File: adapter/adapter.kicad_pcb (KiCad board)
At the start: 2 copper layers, 43.5 x 38.6 mm, 19 parts, among them J2 Conn_01x06_Female, SW1 RotaryEncoder_Switch

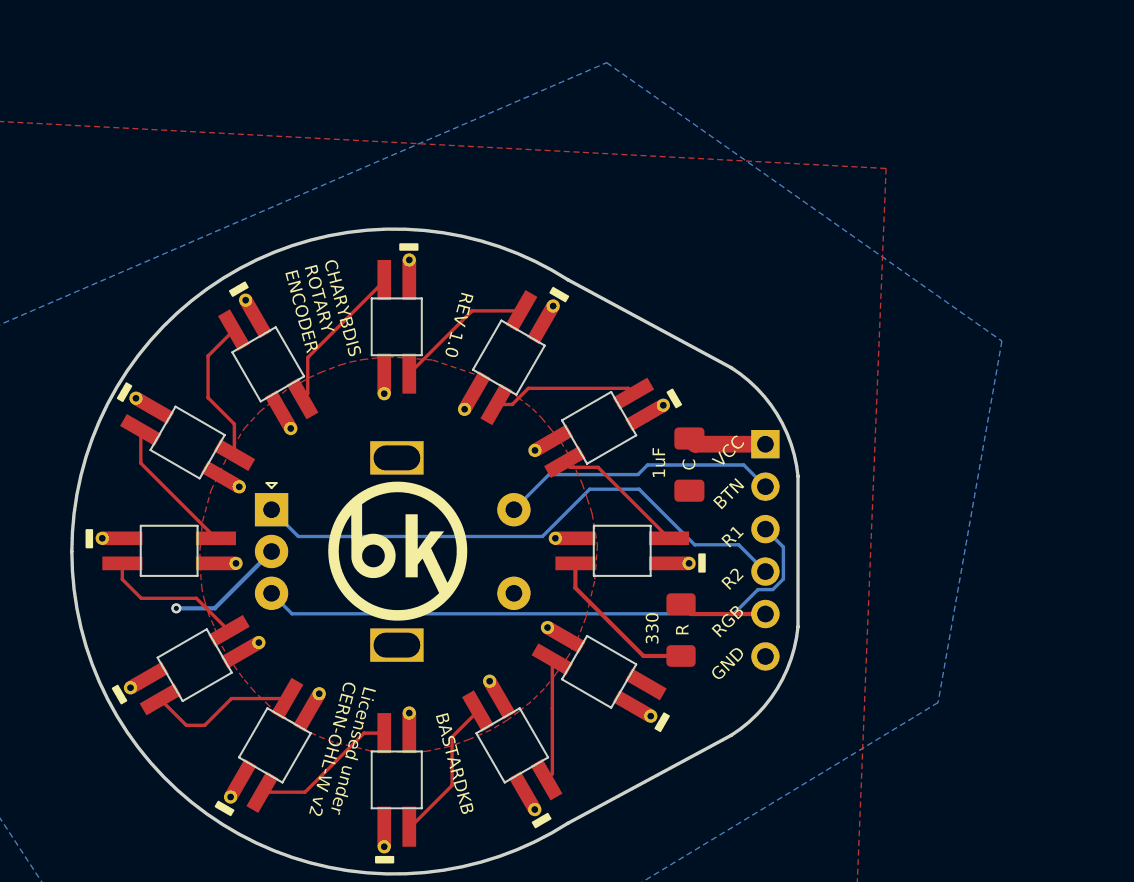
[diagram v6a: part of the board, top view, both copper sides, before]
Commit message: add screw holes
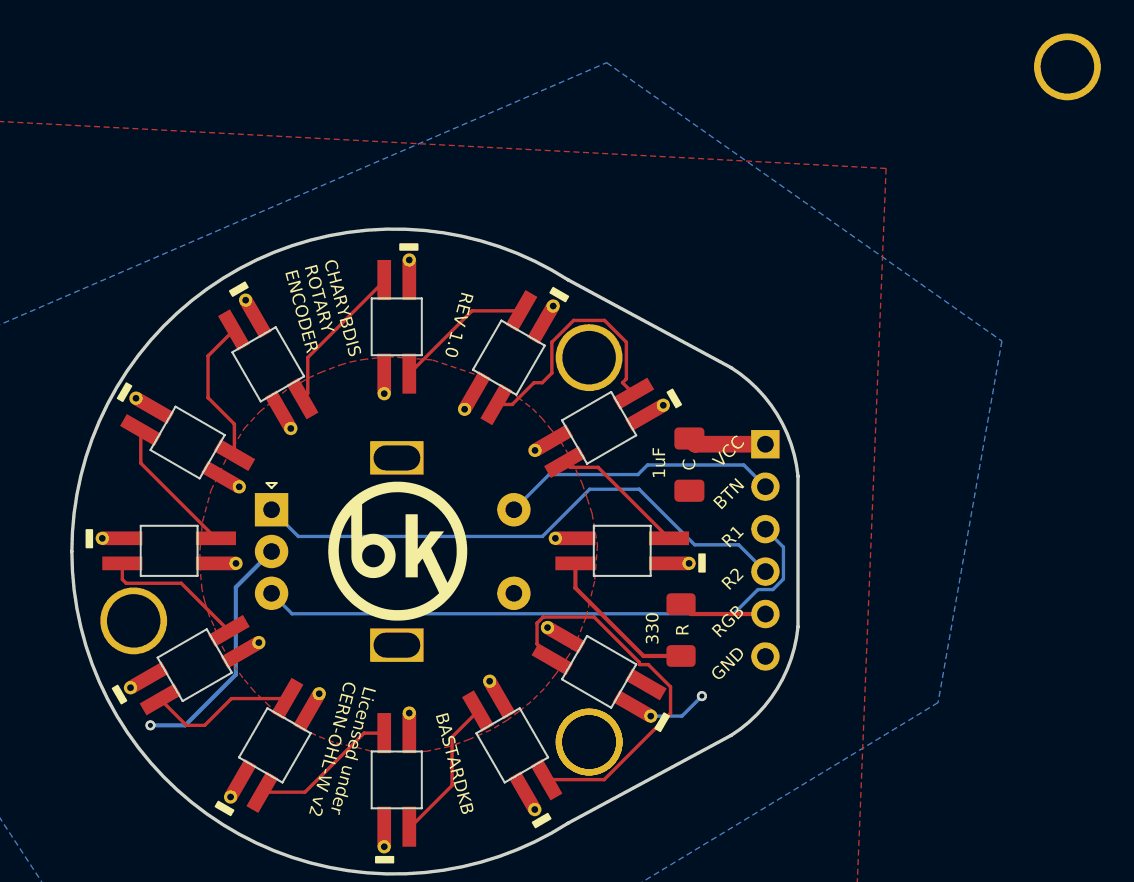
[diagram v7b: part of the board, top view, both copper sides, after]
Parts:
- added ? (x2): , , F.Cu at (64.0, 55.0)
- added ?: , , F.Cu at (92.6, 14.6)
- added ?: , , F.Cu at (36.8, 47.8)
- added ?: , , F.Cu at (64.0, 32.0)
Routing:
- net Net-(D11-Pad3): track 7.35 -> 23.1 mm
- net Gnd: track 7.11 -> 18.2 mm, vias 1 -> 2
- net Net-(D3-Pad1): track 8.73 -> 14.9 mm
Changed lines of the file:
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@@
       ) (layer "F.SilkS") (width 0) (fill solid))
+  )
+  (footprint "" (layer "F.Cu")
+    (at 64 55)
+    (fp_text reference "" (at 0 0) (layer "F.SilkS")
+      (effects (font (size 1.27 1.27) (thickness 0.15)))
+    )
+    (fp_text value "" (at 0 0) (layer "F.SilkS")
+      (effects (font (size 1.27 1.27) (thickness 0.15)))
+    )
+    (pad "1" thru_hole circle locked (at 0 0) (size 4 4) (drill 3.2) (layers *.Cu *.Mask))
   )
   (footprint "Library:YS-SK6812MINI-E" (layer "F.Cu")
@@
       (net 1 "Vcc") (pinfunction "VDD") (pintype "power_in"))
   )
+  (footprint "" (layer "F.Cu")
+    (at 92.62 14.6)
+    (fp_text reference "" (at 0 0) (layer "F.SilkS")
+      (effects (font (size 1.27 1.27) (thickness 0.15)))
+    )
+    (fp_text value "" (at 0 0) (layer "F.SilkS")
+      (effects (font (size 1.27 1.27) (thickness 0.15)))
+    )
+    (pad "1" thru_hole circle locked (at 0 0) (size 4 4) (drill 3.2) (layers *.Cu *.Mask))
+  )
   (footprint "Library:6_PinHeader" locked (layer "F.Cu")
     (at 74.55 43.6)
@@
       (net 1 "Vcc") (pinfunction "VDD") (pintype "power_in"))
   )
+  (footprint "" (layer "F.Cu")
+    (at 64 55)
+    (fp_text reference "" (at 0 0) (layer "F.SilkS")
+      (effects (font (size 1.27 1.27) (thickness 0.15)))
+    )
+    (fp_text value "" (at 0 0) (layer "F.SilkS")
+      (effects (font (size 1.27 1.27) (thickness 0.15)))
+    )
+    (pad "1" thru_hole circle locked (at 0 0) (size 4 4) (drill 3.2) (layers *.Cu *.Mask))
+  )
+  (footprint "" (layer "F.Cu")
+    (at 36.75 47.75)
+    (fp_text reference "" (at 0 0) (layer "F.SilkS")
+      (effects (font (size 1.27 1.27) (thickness 0.15)))
+    )
+    (fp_text value "" (at 0 0) (layer "F.SilkS")
+      (effects (font (size 1.27 1.27) (thickness 0.15)))
+    )
+    (pad "1" thru_hole circle locked (at 0 0) (size 4 4) (drill 3.2) (layers *.Cu *.Mask))
+  )
   (footprint "Resistor_SMD:R_1206_3216Metric_Pad1.30x1.75mm_HandSolder" (layer "F.Cu")
     (at 69.5 48.3 90)
@@
     (pad "4" thru_hole circle (at -4 -0.75 330) (size 0.8 0.8) (drill 0.4) (layers *.Cu *.Mask)
       (net 1 "Vcc") (pinfunction "VDD") (pintype "power_in"))
+  )
+  (footprint "" (layer "F.Cu")
+    (at 64 32)
+    (fp_text reference "" (at 0 0) (layer "F.SilkS")
+      (effects (font (size 1.27 1.27) (thickness 0.15)))
+    )
+    (fp_text value "" (at 0 0) (layer "F.SilkS")
+      (effects (font (size 1.27 1.27) (thickness 0.15)))
+    )
+    (pad "1" thru_hole circle locked (at 0 0) (size 4 4) (drill 3.2) (layers *.Cu *.Mask))
   )
   (footprint "LOGO" (layer "B.Cu")
@@
   (segment (start 70.3425 37.18) (end 70 36.8375) (width 1) (layer "F.Cu") (net 1))
   (segment (start 74.55 37.18) (end 70.3425 37.18) (width 1) (layer "F.Cu") (net 1))
-  (via (at 39.3 47) (size 0.6096) (drill 0.3048) (layers "F.Cu" "B.Cu") (net 2))
-  (segment (start 41.6 47) (end 39.3 47) (width 0.25) (layer "B.Cu") (net 2))
-  (segment (start 45 43.6) (end 41.6 47) (width 0.25) (layer "B.Cu") (net 2))
+  (via (at 37.75 54) (size 0.6096) (drill 0.3048) (layers "F.Cu" "B.Cu") (net 2))
+  (via (at 70.75 52.25) (size 0.6096) (drill 0.3048) (layers "F.Cu" "B.Cu") (net 2))
+  (segment (start 42.863183 50.969184) (end 39.832367 54) (width 0.25) (layer "B.Cu") (net 2))
+  (segment (start 45 43.6) (end 42.863183 45.736817) (width 0.25) (layer "B.Cu") (net 2))
+  (segment (start 67.689102 53.449519) (end 69.550481 53.449519) (width 0.2032) (layer "B.Cu") (net 2))
+  (segment (start 42.863183 45.736817) (end 42.863183 50.969184) (width 0.25) (layer "B.Cu") (net 2))
+  (segment (start 39.832367 54) (end 37.75 54) (width 0.25) (layer "B.Cu") (net 2))
+  (segment (start 69.550481 53.449519) (end 70.75 52.25) (width 0.2032) (layer "B.Cu") (net 2))
   (segment (start 69.5 49.85) (end 67.25 49.85) (width 0.25) (layer "F.Cu") (net 3))
   (segment (start 63.18119 45.78119) (end 63.18119 44.31) (width 0.25) (layer "F.Cu") (net 3))
@@
   (segment (start 64.536056 38.564866) (end 62.865476 38.564866) (width 0.2032) (layer "F.Cu") (net 4))
   (segment (start 68.78119 42.81) (end 64.536056 38.564866) (width 0.2032) (layer "F.Cu") (net 4))
-  (segment (start 66.334524 33.835134) (end 60.364866 33.835134) (width 0.2032) (layer "F.Cu") (net 5))
+  (segment (start 61.771889 32.922915) (end 61.194804 33.5) (width 0.2032) (layer "F.Cu") (net 5))
+  (segment (start 66.228111 33.271279) (end 66.228111 31.077085) (width 0.2032) (layer "F.Cu") (net 5))
   (segment (start 59.400129 34.799871) (end 58.449519 34.799871) (width 0.2032) (layer "F.Cu") (net 5))
-  (segment (start 66.649871 34.150481) (end 66.334524 33.835134) (width 0.2032) (layer "F.Cu") (net 5))
-  (segment (start 60.364866 33.835134) (end 59.400129 34.799871) (width 0.2032) (layer "F.Cu") (net 5))
+  (segment (start 65.99939 33.5) (end 66.228111 33.271279) (width 0.2032) (layer "F.Cu") (net 5))
+  (segment (start 66.228111 31.077085) (end 64.922915 29.771889) (width 0.2032) (layer "F.Cu") (net 5))
+  (segment (start 60.7 33.5) (end 59.400129 34.799871) (width 0.2032) (layer "F.Cu") (net 5))
+  (segment (start 66.649871 34.150481) (end 65.99939 33.5) (width 0.2032) (layer "F.Cu") (net 5))
+  (segment (start 61.771889 31.077085) (end 61.771889 32.922915) (width 0.2032) (layer "F.Cu") (net 5))
+  (segment (start 61.194804 33.5) (end 60.7 33.5) (width 0.2032) (layer "F.Cu") (net 5))
+  (segment (start 64.922915 29.771889) (end 63.077085 29.771889) (width 0.2032) (layer "F.Cu") (net 5))
+  (segment (start 63.077085 29.771889) (end 61.771889 31.077085) (width 0.2032) (layer "F.Cu") (net 5))
   (segment (start 69.5 46.75) (end 70.09 47.34) (width 0.25) (layer "F.Cu") (net 6))
   (segment (start 70.09 47.34) (end 74.55 47.34) (width 0.25) (layer "F.Cu") (net 6))
@@
   (segment (start 53.334305 60.065695) (end 55.8 57.6) (width 0.2032) (layer "F.Cu") (net 9))
   (segment (start 55.8 54.70061) (end 57.350481 53.150129) (width 0.2032) (layer "F.Cu") (net 9))
-  (segment (start 61.800129 52.999871) (end 61.800129 50.049519) (width 0.2032) (layer "F.Cu") (net 10))
-  (segment (start 61.449519 57.249871) (end 61.8 56.89939) (width 0.2032) (layer "F.Cu") (net 10))
-  (segment (start 61.8 53) (end 61.800129 52.999871) (width 0.2032) (layer "F.Cu") (net 10))
-  (segment (start 61.8 56.89939) (end 61.8 53) (width 0.2032) (layer "F.Cu") (net 10))
+  (segment (start 68.872221 53.278805) (end 68.872221 51.700921) (width 0.2032) (layer "F.Cu") (net 10))
+  (segment (start 64.901155 57.249871) (end 68.872221 53.278805) (width 0.2032) (layer "F.Cu") (net 10))
+  (segment (start 60.882787 47.890308) (end 60.882787 49.132177) (width 0.2032) (layer "F.Cu") (net 10))
+  (segment (start 64.298878 47.52237) (end 61.250725 47.52237) (width 0.2032) (layer "F.Cu") (net 10))
+  (segment (start 67.538591 50.367291) (end 67.034833 50.367291) (width 0.2032) (layer "F.Cu") (net 10))
+  (segment (start 61.449519 57.249871) (end 64.901155 57.249871) (width 0.2032) (layer "F.Cu") (net 10))
+  (segment (start 60.882787 49.132177) (end 61.800129 50.049519) (width 0.2032) (layer "F.Cu") (net 10))
+  (segment (start 67.034833 50.367291) (end 66.994948 50.21844) (width 0.2032) (layer "F.Cu") (net 10))
+  (segment (start 61.250725 47.52237) (end 60.882787 47.890308) (width 0.2032) (layer "F.Cu") (net 10))
+  (segment (start 68.872221 51.700921) (end 67.538591 50.367291) (width 0.2032) (layer "F.Cu") (net 10))
+  (segment (start 66.994948 50.21844) (end 64.298878 47.52237) (width 0.2032) (layer "F.Cu") (net 10))
   (segment (start 47.164866 31.995796) (end 47.164866 34.134524) (width 0.2032) (layer "F.Cu") (net 11))
   (segment (start 51.74 27.355088) (end 51.74 27.420662) (width 0.2032) (layer "F.Cu") (net 11))
@@
   (segment (start 37.175787 38.315205) (end 41.670582 42.81) (width 0.2032) (layer "F.Cu") (net 14))
   (segment (start 37.175787 36.329519) (end 37.175787 38.315205) (width 0.2032) (layer "F.Cu") (net 14))
-  (segment (start 40.49939 46.4) (end 42.449871 48.350481) (width 0.2032) (layer "F.Cu") (net 15))
-  (segment (start 36.070582 45.270582) (end 37.2 46.4) (width 0.2032) (layer "F.Cu") (net 15))
+  (segment (start 36.070582 45.270582) (end 36.3 45.5) (width 0.2032) (layer "F.Cu") (net 15))
   (segment (start 36.070582 44.31) (end 36.070582 45.270582) (width 0.2032) (layer "F.Cu") (net 15))
-  (segment (start 37.2 46.4) (end 40.49939 46.4) (width 0.2032) (layer "F.Cu") (net 15))
+  (segment (start 36.3 45.5) (end 39.59939 45.5) (width 0.2032) (layer "F.Cu") (net 15))
+  (segment (start 39.59939 45.5) (end 42.449871 48.350481) (width 0.2032) (layer "F.Cu") (net 15))
   (segment (start 67.495515 38.423489) (end 73.253489 38.423489) (width 0.2) (layer "B.Cu") (net 16))
   (segment (start 66.923489 38.995515) (end 67.495515 38.423489) (width 0.2) (layer "B.Cu") (net 16))

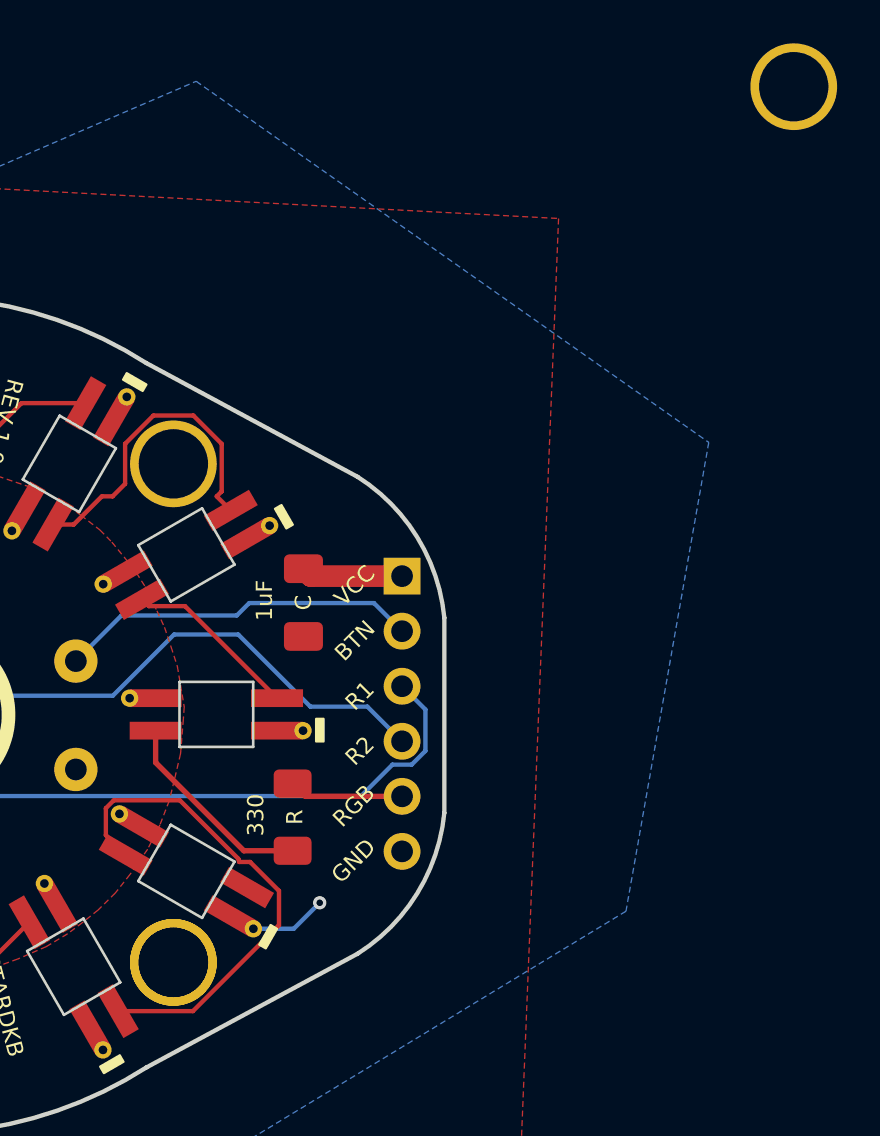
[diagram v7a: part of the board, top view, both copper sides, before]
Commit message: holes fix
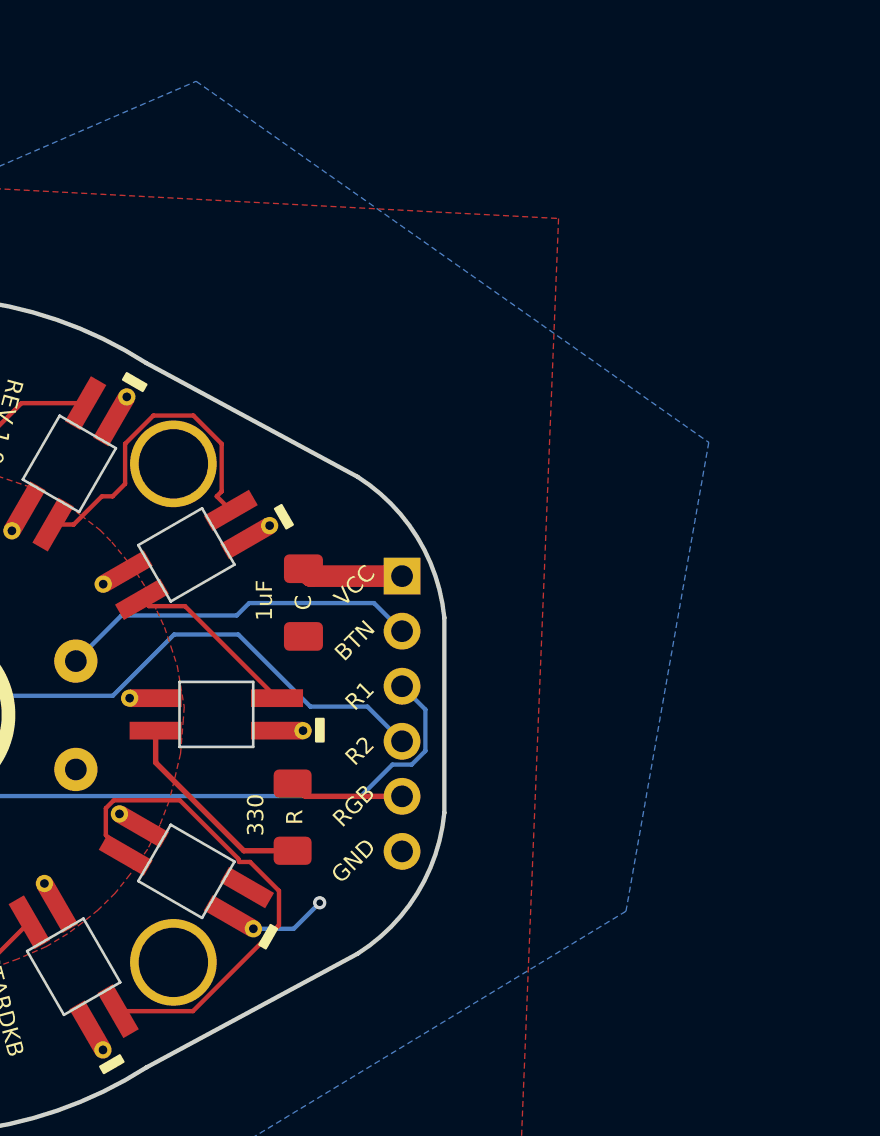
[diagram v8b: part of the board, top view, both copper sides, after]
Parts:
- removed the ? at (64.0, 55.0)
- removed the ? at (92.6, 14.6)
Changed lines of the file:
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@@
       ) (layer "F.SilkS") (width 0) (fill solid))
-  )
-  (footprint "" (layer "F.Cu")
-    (at 64 55)
-    (fp_text reference "" (at 0 0) (layer "F.SilkS")
-      (effects (font (size 1.27 1.27) (thickness 0.15)))
-    )
-    (fp_text value "" (at 0 0) (layer "F.SilkS")
-      (effects (font (size 1.27 1.27) (thickness 0.15)))
-    )
-    (pad "1" thru_hole circle locked (at 0 0) (size 4 4) (drill 3.2) (layers *.Cu *.Mask))
   )
   (footprint "Library:YS-SK6812MINI-E" (layer "F.Cu")
@@
       (net 1 "Vcc") (pinfunction "VDD") (pintype "power_in"))
   )
-  (footprint "" (layer "F.Cu")
-    (at 92.62 14.6)
-    (fp_text reference "" (at 0 0) (layer "F.SilkS")
-      (effects (font (size 1.27 1.27) (thickness 0.15)))
-    )
-    (fp_text value "" (at 0 0) (layer "F.SilkS")
-      (effects (font (size 1.27 1.27) (thickness 0.15)))
-    )
-    (pad "1" thru_hole circle locked (at 0 0) (size 4 4) (drill 3.2) (layers *.Cu *.Mask))
-  )
   (footprint "Library:6_PinHeader" locked (layer "F.Cu")
